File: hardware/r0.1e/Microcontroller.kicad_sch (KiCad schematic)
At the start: 95 parts, among them J10 UART, J2 USB_C, J3 OLED, J8 +12V, J9 STLink, Q4 IRLML2244, Q5 MMBT3904, SW1 Button Up, SW2 Button Down, SW3 Reset, SW4 Button Escape, SW5 Button Left, SW6 Button Enter, SW7 Button Right, SW8 Button Power, U10 STM32F405RGTx, U11 TPS73233, U2 TP6841S6, U3 USBLC6-2, X1 12 MHz TCXO, Y1 8 MHz

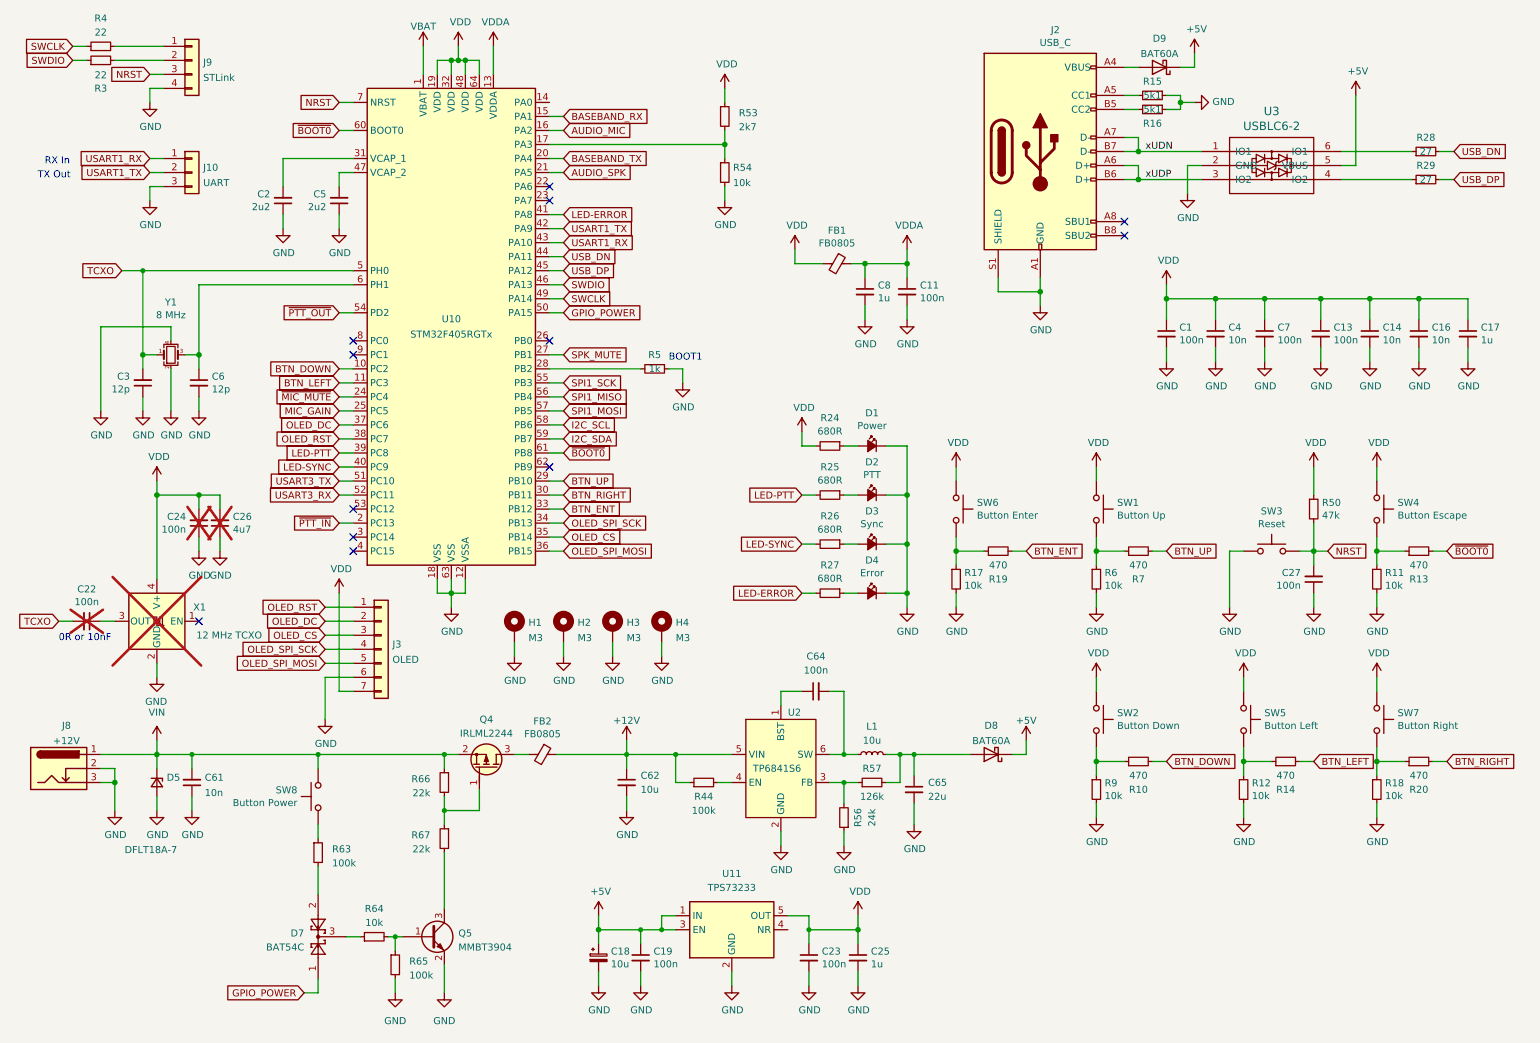
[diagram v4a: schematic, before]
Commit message: Finished MPN for r0.1e
Targeted towards LCSC/JLCPCB
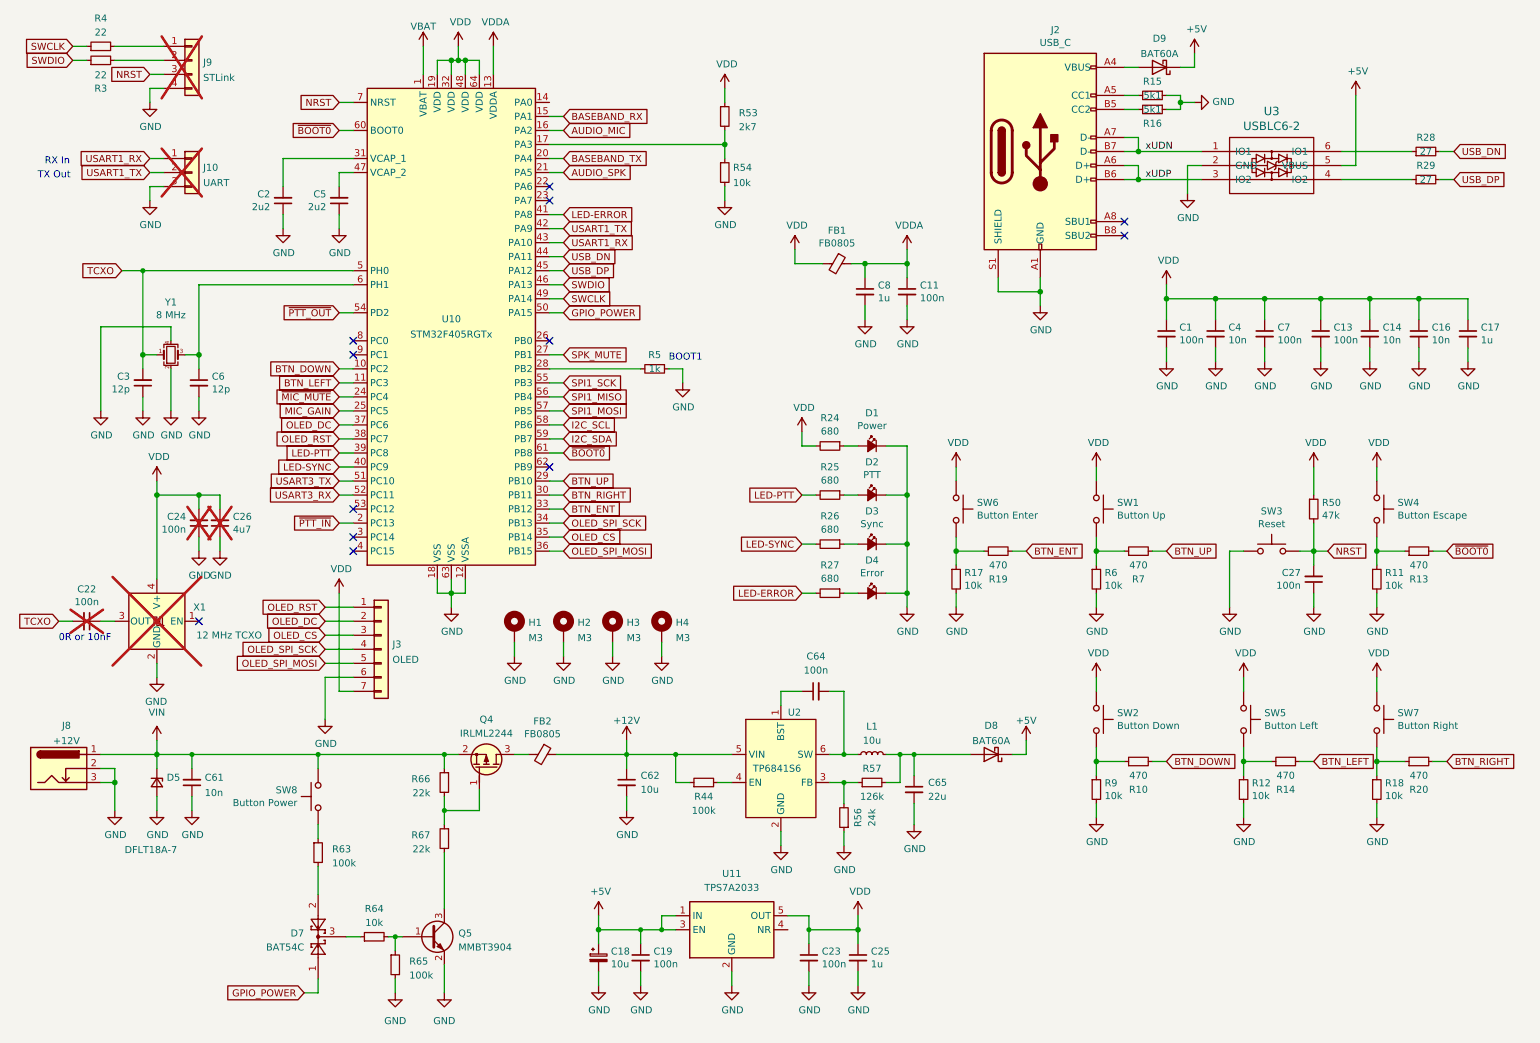
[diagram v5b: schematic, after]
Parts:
- C1, C11, C13, C19, C22, C23, C24, C27, C64, C7: MPN (none) -> Generic C/100nF/C0G/25V/0603
- C14, C16, C4, C61: MPN (none) -> Generic C/10nF/C0G/25V/0603
- C17, C25, C8: MPN (none) -> Generic C/1uF/C0G/25V/0603
- C18: MPN (none) -> T491A106K016AT
- C2, C5: MPN (none) -> Generic C/2.2uF/C0G/25V/0603
- C3, C6: MPN (none) -> Generic C/12pF/C0G/16V/0603
- C62: MPN (none) -> Generic C/10uF/C0G/25V/1210
- C65: MPN (none) -> Generic C/22uF/C0G/10V/1210
- D1: MPN (none) -> Generic LED/Blue/0603
- D2: MPN (none) -> Generic LED/Red/0603
- D3: MPN (none) -> Generic LED/Green/0603
- D4: MPN (none) -> Generic LED/Orange/0603
- D7: MPN (none) -> BAT54CLT11G
- D9: MPN (none) -> BAT60AE6327HTSA1
- FB1, FB2: MPN (none) -> 2508056017Y2
- H1, H2, H3, H4: now left out of the parts list
- J10, J9: now not fitted; now left out of the parts list
- J2: MPN (none) -> TYPE-C-31-M-12
- J3: MPN (none) -> PZ254V-11-07P
- J8: MPN FC681465ST -> DC-005-5A-2.5-SMT
- Q5: MPN MMBT3904 -> SMMBT3904LT1G
- R10, R13, R14, R19, R20, R7: MPN (none) -> Generic R/470R/0603
- R11, R12, R17, R18, R54, R6, R64, R9: MPN (none) -> Generic R/10k/0603
- R15, R16: MPN (none) -> Generic R/5k1/0603
- R24, R25, R26, R27: value 680R -> 680; MPN (none) -> Generic R/680R/0603
- R28, R29: MPN (none) -> Generic R/27R/0603
- R3, R4: MPN (none) -> Generic R/22R/0603
- R44, R63, R65: MPN (none) -> Generic R/100k/0603
- R5: MPN (none) -> Generic R/1k/0603
- R50: MPN (none) -> Generic R/47k/0603
- R53: MPN (none) -> Generic R/2k7/0603
- R56: MPN (none) -> Generic R/24k/0603
- R57: MPN (none) -> Generic R/126k/0603
- R66, R67: MPN (none) -> Generic R/22k/0603
- SW1, SW2, SW4, SW5, SW6, SW7, SW8: MPN (none) -> PTS645SH50SMTR92LFS
- SW3: MPN (none) -> ST-1185SE
- U10: MPN STM32F405RGTx -> STM32F405RGT6V
- U11: value TPS73233 -> TPS7A2033; MPN (none) -> TPS7A2033PDBVR
- U2: MPN (none) -> TP6841S6
- Y1: MPN (none) -> ECS-80-12-33-JGN-TR

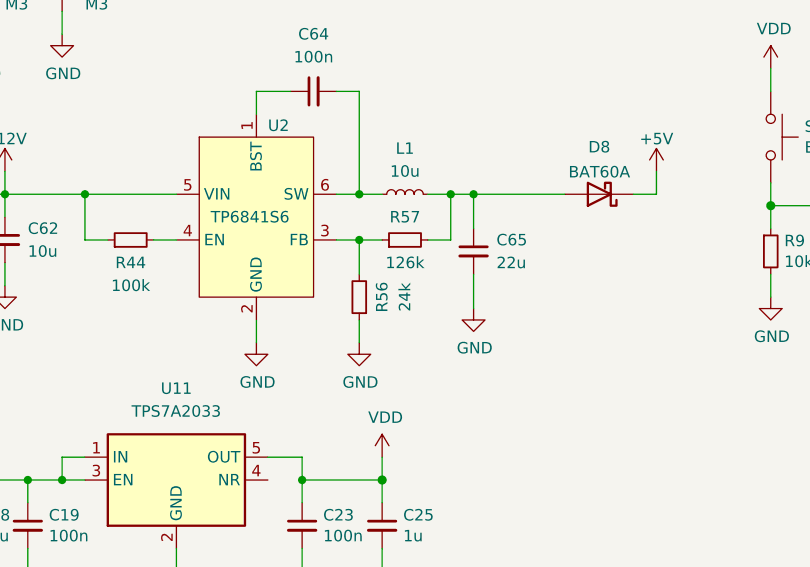
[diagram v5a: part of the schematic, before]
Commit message: r0.1e PCBA files
specifically for JLCPCB
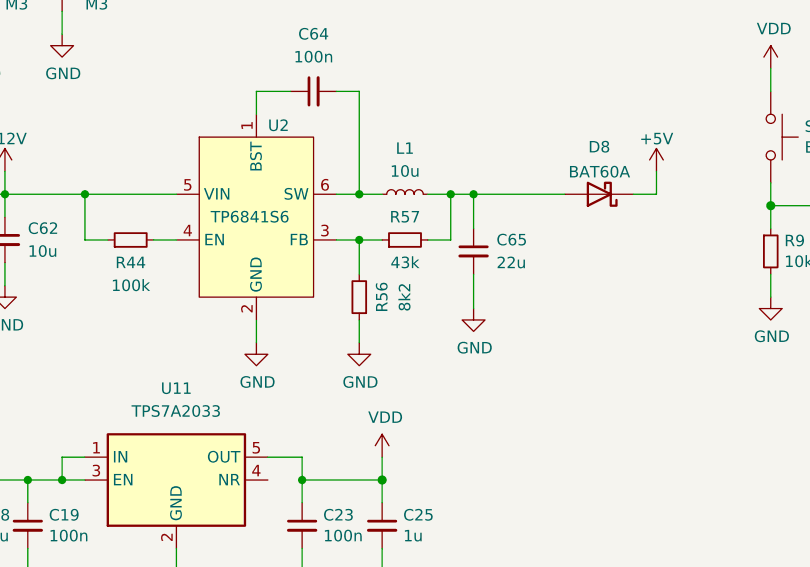
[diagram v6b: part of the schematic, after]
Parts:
- C18: LCSC Part # (none) -> C110055
- D5: LCSC Part # (none) -> C2909295; now left out of the parts list
- D7: LCSC Part # (none) -> C2135
- D8, D9: LCSC Part # (none) -> C520634
- FB1, FB2: LCSC Part # (none) -> C1017
- J2: LCSC Part # (none) -> C165948
- J3: LCSC Part # (none) -> C492406
- J8: LCSC Part # (none) -> C319133
- L1: LCSC Part # (none) -> C506573; MPN IHLP2525CZER100M01 -> IHLP2525BDER100M01
- Q4: LCSC Part # (none) -> C169763
- Q5: LCSC Part # (none) -> C84555
- R56: value 24k -> 8k2; MPN Generic R/24k/0603 -> Generic R/8k2/0603
- R57: value 126k -> 43k; MPN Generic R/126k/0603 -> Generic R/43k/0603
- SW1, SW2, SW4, SW5, SW6, SW7, SW8: LCSC Part # (none) -> C83916
- SW3: LCSC Part # (none) -> C589193
- U10: LCSC Part # (none) -> C15742
- U11: LCSC Part # (none) -> C2862740
- U2: LCSC Part # (none) -> C2844924
- U3: LCSC Part # (none) -> C7519
- Y1: LCSC Part # (none) -> C518156
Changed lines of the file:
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@@
       (effects (font (size 1.27 1.27)) hide)
     )
+    (property "LCSC Part #" "C518156" (at 40.64 74.93 0)
+      (effects (font (size 1.27 1.27)) hide)
+    )
     (pin "1")
     (pin "2")
@@
       (effects (font (size 1.27 1.27)) hide)
     )
+    (property "LCSC Part #" "C1017" (at 161.29 58.42 0)
+      (effects (font (size 1.27 1.27)) hide)
+    )
     (pin "1")
     (pin "2")
@@
       (effects (font (size 1.27 1.27)) hide)
     )
+    (property "LCSC Part #" "C589193" (at 240.03 110.49 0)
+      (effects (font (size 1.27 1.27)) hide)
+    )
     (pin "1")
     (pin "2")
@@
       (effects (font (size 1.27 1.27)) hide)
     )
+    (property "LCSC Part #" "C83916" (at 208.28 102.87 0)
+      (effects (font (size 1.27 1.27)) hide)
+    )
     (pin "1")
     (pin "2")
@@
       (effects (font (size 1.27 1.27)) hide)
     )
+    (property "LCSC Part #" "C83916" (at 259.08 102.87 0)
+      (effects (font (size 1.27 1.27)) hide)
+    )
     (pin "1")
     (pin "2")
@@
       (effects (font (size 1.27 1.27)) hide)
     )
+    (property "LCSC Part #" "C83916" (at 208.28 140.97 0)
+      (effects (font (size 1.27 1.27)) hide)
+    )
     (pin "1")
     (pin "2")
@@
       (effects (font (size 1.27 1.27)) hide)
     )
+    (property "LCSC Part #" "C83916" (at 182.88 102.87 0)
+      (effects (font (size 1.27 1.27)) hide)
+    )
     (pin "1")
     (pin "2")
@@
       (effects (font (size 1.27 1.27)) hide)
     )
+    (property "LCSC Part #" "C83916" (at 234.95 140.97 0)
+      (effects (font (size 1.27 1.27)) hide)
+    )
     (pin "1")
     (pin "2")
@@
       (effects (font (size 1.27 1.27)) hide)
     )
+    (property "LCSC Part #" "C83916" (at 259.08 140.97 0)
+      (effects (font (size 1.27 1.27)) hide)
+    )
     (pin "1")
     (pin "2")
@@
       (effects (font (size 1.27 1.27)) hide)
     )
+    (property "LCSC Part #" "C165948" (at 198.12 38.1 0)
+      (effects (font (size 1.27 1.27)) hide)
+    )
     (pin "A1")
     (pin "A12")
@@
       (effects (font (size 1.27 1.27)) hide)
     )
+    (property "LCSC Part #" "C7519" (at 240.03 40.64 0)
+      (effects (font (size 1.27 1.27)) hide)
+    )
     (pin "1")
     (pin "2")
@@
       (effects (font (size 1.27 1.27)) hide)
     )
+    (property "LCSC Part #" "C110055" (at 118.11 184.15 0)
+      (effects (font (size 1.27 1.27)) hide)
+    )
     (pin "1")
     (pin "2")
@@
       (effects (font (size 1.27 1.27)) hide)
     )
+    (property "LCSC Part #" "C2862740" (at 142.24 179.07 0)
+      (effects (font (size 1.27 1.27)) hide)
+    )
     (pin "1")
     (pin "2")
@@
       (effects (font (size 1.27 1.27)))
     )
-    (property "Value" "24k" (at 167.64 158.75 90)
+    (property "Value" "8k2" (at 167.64 158.75 90)
       (effects (font (size 1.27 1.27)))
     )
@@
       (effects (font (size 1.524 1.524)))
     )
-    (property "MPN" "Generic R/24k/0603" (at 162.56 158.75 0)
+    (property "MPN" "Generic R/8k2/0603" (at 162.56 158.75 0)
       (effects (font (size 1.27 1.27)) hide)
     )
@@
       (effects (font (size 1.27 1.27)) hide)
     )
+    (property "LCSC Part #" "C492406" (at 78.74 128.27 0)
+      (effects (font (size 1.27 1.27)) hide)
+    )
     (pin "1")
     (pin "2")
@@
       (effects (font (size 1.27 1.27)) hide)
     )
+    (property "LCSC Part #" "C319133" (at 20.32 149.86 0)
+      (effects (font (size 1.27 1.27)) hide)
+    )
     (pin "1")
     (pin "2")
@@
   )
   (symbol (lib_id "Device:D_Zener_Small") (at 38.1 152.4 270) (unit 1)
-    (in_bom yes) (on_board yes) (dnp no)
+    (in_bom no) (on_board yes) (dnp no)
     (property "Reference" "D5" (at 39.8781 151.4915 90)
       (effects (font (size 1.27 1.27)) (justify left))
@@
       (effects (font (size 1.27 1.27)) hide)
     )
+    (property "LCSC Part #" "C2909295" (at 38.1 152.4 0)
+      (effects (font (size 1.27 1.27)) hide)
+    )
     (pin "1")
     (pin "2")
@@
       (effects (font (size 1.524 1.524)))
     )
-    (property "MPN" "IHLP2525CZER100M01" (at 167.64 147.32 0)
+    (property "MPN" "IHLP2525BDER100M01" (at 167.64 147.32 0)
+      (effects (font (size 1.27 1.27)) hide)
+    )
+    (property "LCSC Part #" " C506573" (at 167.64 147.32 0)
       (effects (font (size 1.27 1.27)) hide)
     )
@@
       (effects (font (size 1.27 1.27)) hide)
     )
+    (property "LCSC Part #" "C520634" (at 219.71 22.86 0)
+      (effects (font (size 1.27 1.27)) hide)
+    )
     (pin "1")
     (pin "2")
@@
       (effects (font (size 1.27 1.27)) hide)
     )
+    (property "LCSC Part #" "C84555" (at 87.63 180.34 0)
+      (effects (font (size 1.27 1.27)) hide)
+    )
     (pin "1")
     (pin "2")
@@
       (effects (font (size 1.27 1.27)) hide)
     )
+    (property "LCSC Part #" "C15742" (at 91.44 69.85 0)
+      (effects (font (size 1.27 1.27)) hide)
+    )
     (pin "1")
     (pin "10")
@@
       (effects (font (size 1.27 1.27)) hide)
     )
+    (property "LCSC Part #" "C520634" (at 189.23 147.32 0)
+      (effects (font (size 1.27 1.27)) hide)
+    )
     (pin "1")
     (pin "2")
@@
       (effects (font (size 1.27 1.27)))
     )
-    (property "Value" "126k" (at 167.64 154.94 90)
+    (property "Value" "43k" (at 167.64 154.94 90)
       (effects (font (size 1.27 1.27)))
     )
@@
       (effects (font (size 1.524 1.524)))
     )
-    (property "MPN" "Generic R/126k/0603" (at 167.64 152.4 0)
+    (property "MPN" "Generic R/43k/0603" (at 167.64 152.4 0)
       (effects (font (size 1.27 1.27)) hide)
     )
@@
       (effects (font (size 1.27 1.27)) hide)
     )
+    (property "LCSC Part #" "C2844924" (at 151.13 149.86 0)
+      (effects (font (size 1.27 1.27)) hide)
+    )
     (pin "1")
     (pin "2")
@@
       (effects (font (size 1.27 1.27)) hide)
     )
+    (property "LCSC Part #" "C2135" (at 67.31 180.34 0)
+      (effects (font (size 1.27 1.27)) hide)
+    )
     (pin "1")
     (pin "2")
@@
       (effects (font (size 1.27 1.27)) hide)
     )
+    (property "LCSC Part #" "C83916" (at 67.31 154.94 0)
+      (effects (font (size 1.27 1.27)) hide)
+    )
     (pin "1")
     (pin "2")
@@
       (effects (font (size 1.27 1.27)) hide)
     )
+    (property "LCSC Part #" "C169763" (at 97.79 149.86 0)
+      (effects (font (size 1.27 1.27)) hide)
+    )
     (pin "1")
     (pin "2")
@@
       (effects (font (size 1.27 1.27)) hide)
     )
+    (property "LCSC Part #" "C1017" (at 107.95 147.32 0)
+      (effects (font (size 1.27 1.27)) hide)
+    )
